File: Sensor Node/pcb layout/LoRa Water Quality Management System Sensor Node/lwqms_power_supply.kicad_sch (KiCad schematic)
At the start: 6 parts, among them U3 TPS631010YBGR

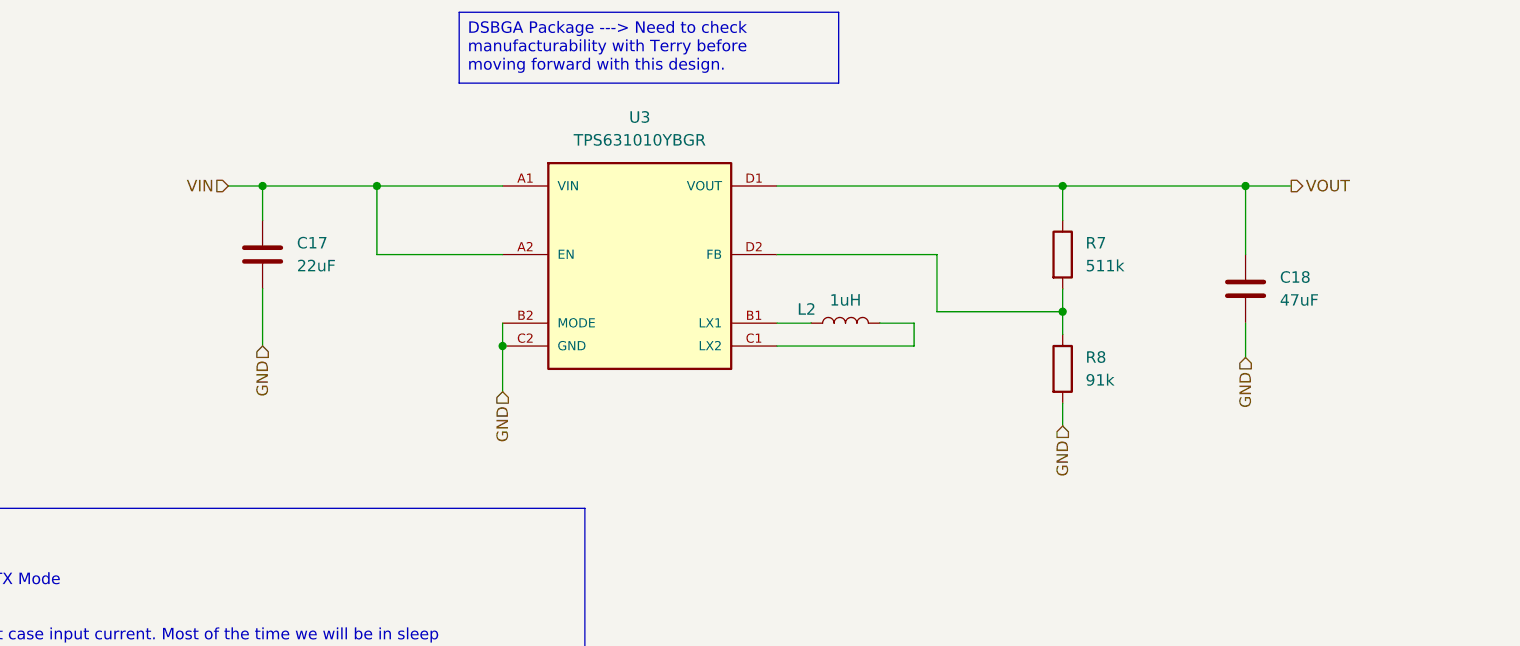
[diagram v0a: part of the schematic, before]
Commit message: Add finalized schematics for sx1262 and SPI flash.
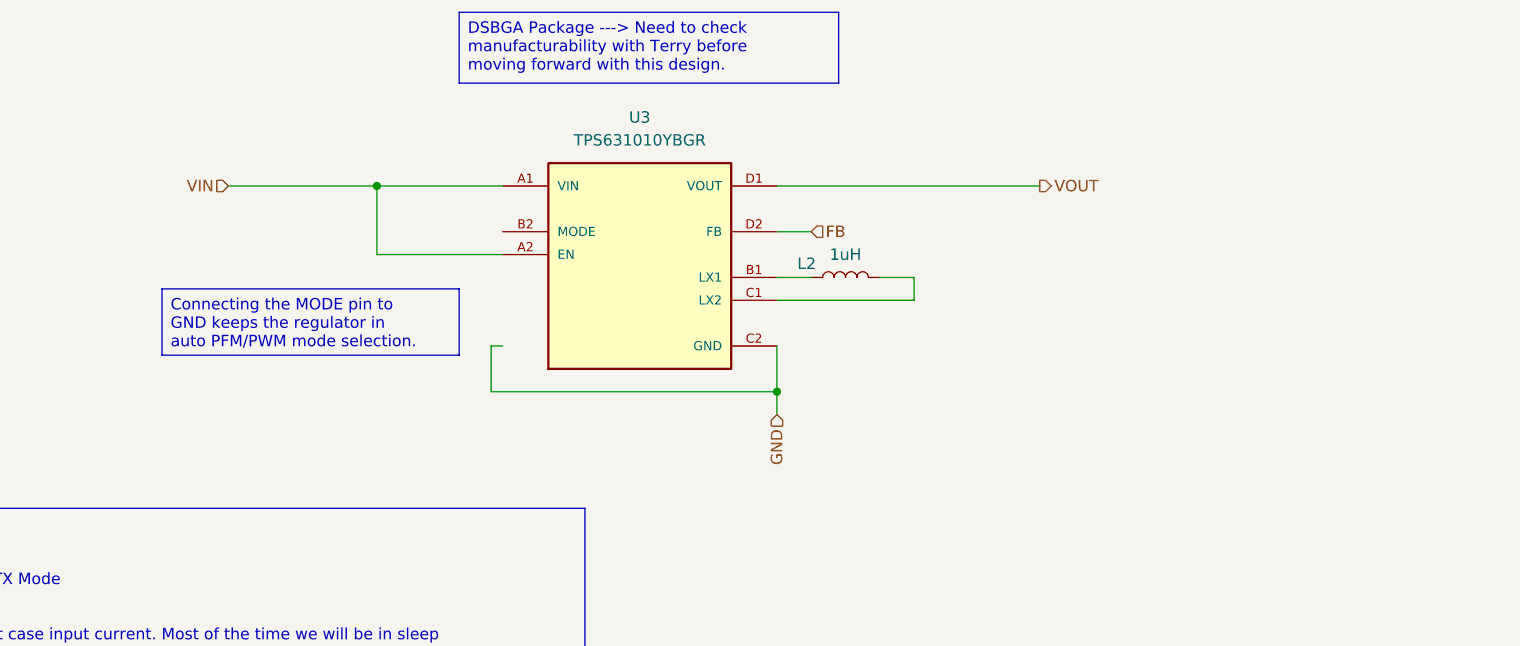
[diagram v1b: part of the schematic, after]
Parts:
- removed C17: 22uF, symbol Device:C
- removed C18: 47uF, symbol Device:C
- removed R7: 511k, symbol Device:R
- removed R8: 91k, symbol Device:R
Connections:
- net GND: no longer U3.B2 (MODE)
- net FB: now reaches U3.D2 (FB)
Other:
- moved on the sheet: L2

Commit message: Finalize first draft schematic capture, assign all footprints, and begin preliminary PCB layout.
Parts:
- L2: footprint (none) -> Inductor_SMD:L_1008_2520Metric_Pad1.43x2.20mm_HandSolder
- U9: renamed from U3; footprint TPS631010YBGR:IC_TPS631010YBGR -> LWQMS:IC_TPS631010YBGR
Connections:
- net GND: now also U9.B2 (MODE)
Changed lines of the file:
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@@
-		)
-	)
-	(text_box "DSBGA Package ---> Need to check manufacturability with Terry before moving forward with this design."
-		(exclude_from_sim no)
-		(at 123.444 56.896 0)
-		(size 42.164 7.874)
-		(margins 0.9525 0.9525 0.9525 0.9525)
-		(stroke
-			(width 0)
-			(type solid)
-		)
-		(fill
-			(type none)
-		)
-		(effects
-			(font
-				(size 1.27 1.27)
-			)
-			(justify left top)
 		)
 	)
@@
 	(wire
 		(pts
+			(xy 127 99.06) (xy 127 81.28)
+		)
+		(stroke
+			(width 0)
+			(type default)
+		)
+	)
+	(wire
+		(pts
 			(xy 158.75 88.9) (xy 173.99 88.9)
 		)
@@
 	(wire
 		(pts
-			(xy 128.27 93.98) (xy 127 93.98)
-		)
-		(stroke
-			(width 0)
-			(type default)
-		)
-	)
-	(wire
-		(pts
 			(xy 173.99 86.36) (xy 173.99 88.9)
 		)
@@
 	(wire
 		(pts
-			(xy 127 93.98) (xy 127 99.06)
+			(xy 127 81.28) (xy 128.27 81.28)
 		)
 		(stroke
@@
 			)
 		)
-		(property "Footprint" ""
+		(property "Footprint" "Inductor_SMD:L_1008_2520Metric_Pad1.43x2.20mm_HandSolder"
 			(at 166.37 86.36 0)
 			(effects
@@
 			)
 		)
-		(property "Datasheet" "~"
+		(property "Datasheet" "kicad-embed://m_dfe252012p.pdf"
 			(at 166.37 86.36 0)
 			(effects
@@
 			)
 		)
-		(property "Description" "Inductor"
+		(property "Description" "DFE252012P-1R0M=P2"
 			(at 166.37 86.36 0)
 			(effects
@@
 		(dnp no)
 		(fields_autoplaced yes)
-		(property "Reference" "U3"
+		(property "Reference" "U9"
 			(at 143.51 68.58 0)
 			(effects
@@
 			)
 		)
-		(property "Footprint" "TPS631010YBGR:IC_TPS631010YBGR"
+		(property "Footprint" "LWQMS:IC_TPS631010YBGR"
 			(at 143.51 86.36 0)
 			(effects
@@
 			(project "LoRa Water Quality Management System Sensor Node"
 				(path "/f090528b-8c52-4bf9-a2b8-0c17aa5e5727/33bb74cb-874c-4792-9754-f72a20576d07"
-					(reference "U3")
+					(reference "U9")
 					(unit 1)
 				)
 				(path "/f090528b-8c52-4bf9-a2b8-0c17aa5e5727/e40534b4-86b2-44fa-9b4b-4985bdae1c57"
-					(reference "U4")
+					(reference "U10")
 					(unit 1)
 				)

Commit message: Add preliminary changes based on feedback from Zach Martin.
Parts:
- removed U9: TPS631010YBGR, LWQMS:IC_TPS631010YBGR, symbol LoRaWaterQualityManagementSystem:TPS631010YBGR
- added C37: 100n, Capacitor_SMD:C_0805_2012Metric_Pad1.18x1.45mm_HandSolder, symbol Device:C
- added R39: 100R, Resistor_SMD:R_0805_2012Metric_Pad1.20x1.40mm_HandSolder, symbol Device:R
- added U9: TPS63000, symbol Regulator_Switching:TPS63000
- L2: value 1uH -> 2.2uH; footprint Inductor_SMD:L_1008_2520Metric_Pad1.43x2.20mm_HandSolder -> (none); MFG P/N (none) -> LQH3NPZ2R2MMEL
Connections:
- net FB: now also U9.10 (FB)
- net GND: now also C37.2, U9.11 (PGND), U9.3 (PGND), U9.9 (GND)
- net VIN: now also R39.1, U9.5 (VIN)
- net VOUT: now also U9.1 (VOUT)
- net at L2.1: now also U9.4 (L1)
- net at L2.2: now also U9.2 (L2)
- new net: C37.1, R39.2, U9.6 (EN), U9.7 (PS/SYNC), U9.8 (VINA)

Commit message: oops
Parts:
- L2: footprint (none) -> LWQMS:IND_LQH3NPZ2R2MMEL
- U9: footprint (none) -> LWQMS:CONV_TPS63000DRCR
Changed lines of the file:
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@@
 			)
 		)
-		(property "Footprint" ""
+		(property "Footprint" "LWQMS:IND_LQH3NPZ2R2MMEL"
 			(at 170.18 115.57 0)
 			(effects
@@
 			)
 		)
-		(property "Footprint" ""
+		(property "Footprint" "LWQMS:CONV_TPS63000DRCR"
 			(at 204.47 124.46 0)
 			(effects

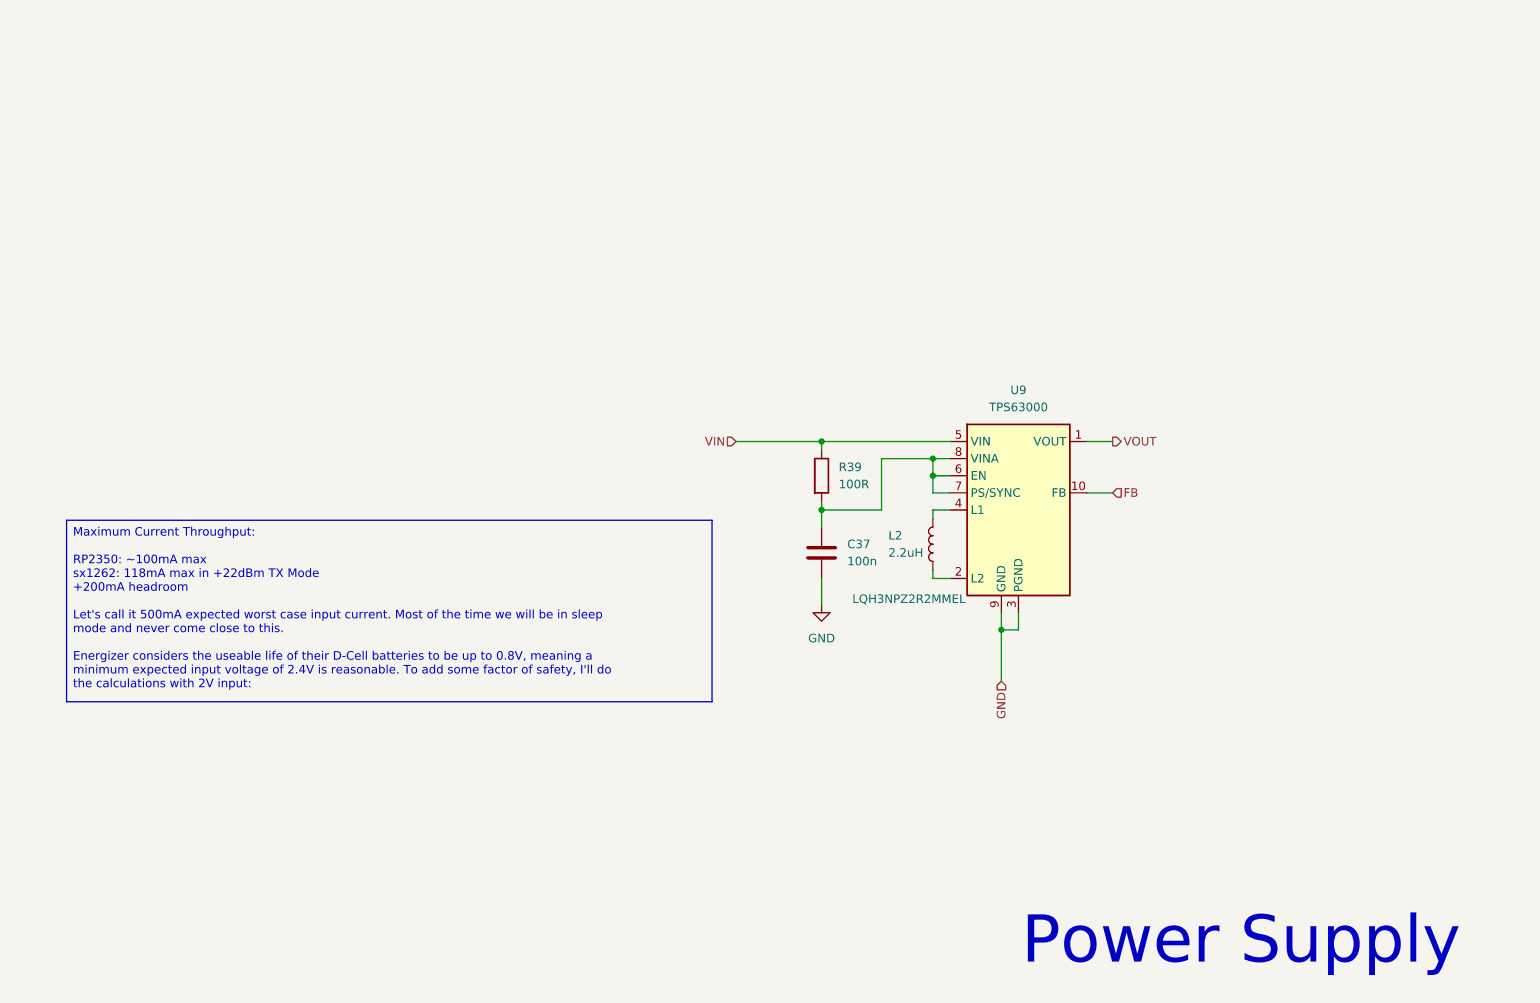
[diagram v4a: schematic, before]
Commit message: Update all R/C components to 0805, complete layout of updated buck-boost converter. Add TVS diodes for ESD protection on vulnerable signals, add reference designators, and fix clearance issues.
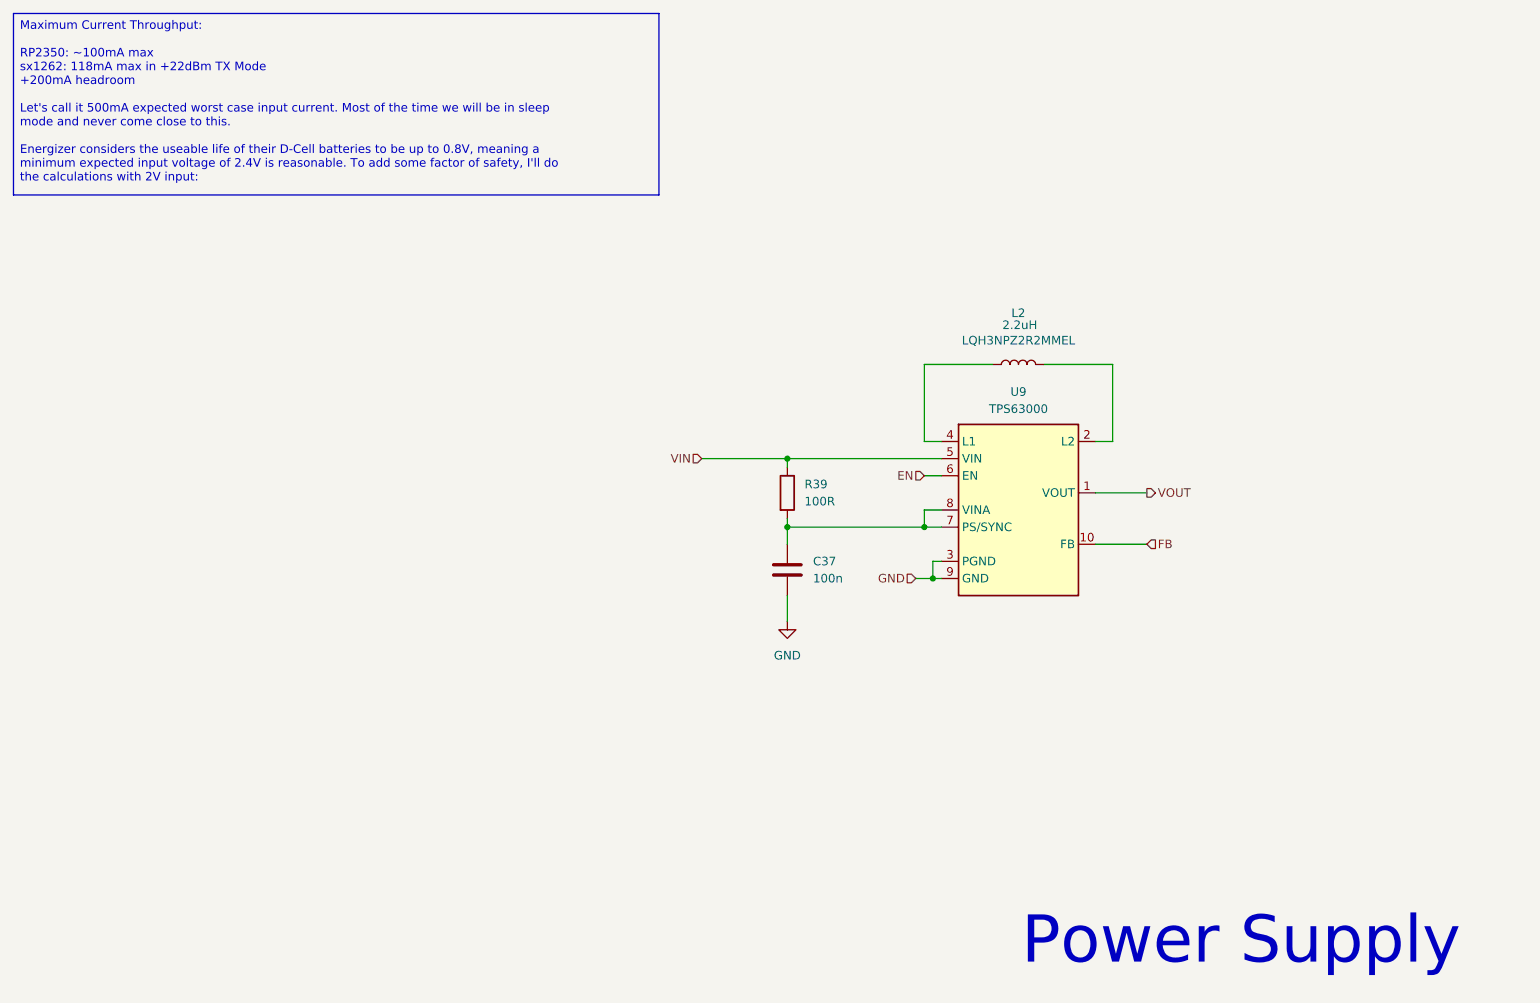
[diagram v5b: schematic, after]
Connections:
- net GND: now also U9.11_1 (PGND), U9.11_2 (PGND), U9.11_3 (PGND), U9.11_4 (PGND), U9.11_5 (PGND), U9.11_6 (PGND), U9.11_7 (PGND), U9.11_8 (PGND)
- net at C37.1, R39.2, U9.7 (PS/SYNC)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: no longer U9.6 (EN)
- net at L2.1: now also U9.2 (L2); no longer U9.4 (L1)
- net at L2.2: now also U9.4 (L1); no longer U9.2 (L2)
- new net EN: U9.6 (EN)
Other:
- moved on the sheet: C37, L2, R39, U9

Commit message: Finalize PCB for order
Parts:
- renumbered C37 to C33, L2 to L3, R39 to R27
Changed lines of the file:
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@@
 		(dnp no)
 		(fields_autoplaced yes)
-		(property "Reference" "R39"
+		(property "Reference" "R27"
 			(at 151.13 106.6799 0)
 			(effects
@@
 		)
 		(property "Description" "Resistor"
+			(at 148.59 107.95 0)
+			(effects
+				(font
+					(size 1.27 1.27)
+				)
+				(hide yes)
+			)
+		)
+		(property "SNAPEDA_PACKAGE_ID" ""
 			(at 148.59 107.95 0)
 			(effects
@@
 			(project ""
 				(path "/f090528b-8c52-4bf9-a2b8-0c17aa5e5727/33bb74cb-874c-4792-9754-f72a20576d07"
-					(reference "R39")
+					(reference "R27")
 					(unit 1)
 				)
 				(path "/f090528b-8c52-4bf9-a2b8-0c17aa5e5727/e40534b4-86b2-44fa-9b4b-4985bdae1c57"
-					(reference "R40")
+					(reference "R28")
 					(unit 1)
 				)
@@
 		(dnp no)
 		(fields_autoplaced yes)
-		(property "Reference" "C37"
+		(property "Reference" "C33"
 			(at 152.4 118.1099 0)
 			(effects
@@
 		)
 		(property "Description" "Unpolarized capacitor"
+			(at 148.59 119.38 0)
+			(effects
+				(font
+					(size 1.27 1.27)
+				)
+				(hide yes)
+			)
+		)
+		(property "SNAPEDA_PACKAGE_ID" ""
 			(at 148.59 119.38 0)
 			(effects
@@
 			(project ""
 				(path "/f090528b-8c52-4bf9-a2b8-0c17aa5e5727/33bb74cb-874c-4792-9754-f72a20576d07"
-					(reference "C37")
+					(reference "C33")
 					(unit 1)
 				)
 				(path "/f090528b-8c52-4bf9-a2b8-0c17aa5e5727/e40534b4-86b2-44fa-9b4b-4985bdae1c57"
-					(reference "C38")
+					(reference "C34")
 					(unit 1)
 				)
@@
 		(dnp no)
 		(fields_autoplaced yes)
-		(property "Reference" "#PWR082"
+		(property "Reference" "#PWR066"
 			(at 148.59 133.35 0)
 			(effects
@@
 			(project ""
 				(path "/f090528b-8c52-4bf9-a2b8-0c17aa5e5727/33bb74cb-874c-4792-9754-f72a20576d07"
-					(reference "#PWR082")
+					(reference "#PWR066")
 					(unit 1)
 				)
 				(path "/f090528b-8c52-4bf9-a2b8-0c17aa5e5727/e40534b4-86b2-44fa-9b4b-4985bdae1c57"
-					(reference "#PWR083")
+					(reference "#PWR067")
 					(unit 1)
 				)
@@
 		(on_board yes)
 		(dnp no)
-		(property "Reference" "L2"
+		(property "Reference" "L3"
 			(at 183.896 81.28 90)
 			(effects
@@
 					(size 1.27 1.27)
 				)
+			)
+		)
+		(property "SNAPEDA_PACKAGE_ID" ""
+			(at 182.88 88.9 90)
+			(effects
+				(font
+					(size 1.27 1.27)
+				)
+				(hide yes)
 			)
 		)
@@
 			(project ""
 				(path "/f090528b-8c52-4bf9-a2b8-0c17aa5e5727/33bb74cb-874c-4792-9754-f72a20576d07"
-					(reference "L2")
+					(reference "L3")
 					(unit 1)
 				)
 				(path "/f090528b-8c52-4bf9-a2b8-0c17aa5e5727/e40534b4-86b2-44fa-9b4b-4985bdae1c57"
-					(reference "L3")
+					(reference "L4")
 					(unit 1)
 				)
@@
 			(at 182.88 110.49 0)
 			(effects
+				(font
+					(size 1.27 1.27)
+				)
+				(hide yes)
+			)
+		)
+		(property "SNAPEDA_PACKAGE_ID" ""
+			(at 182.88 110.49 0)
+			(effects
